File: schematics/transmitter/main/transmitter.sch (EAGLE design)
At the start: 103 parts, among them Q1 16MHz, Q2 P_MOSFET, T1 BC337, T2 BC337, T3 BC337, T4 BC337, U1 EEPROM-I2C, U2 AMS1117_5V, U3 AMS1117_5V, U4 ATMEGA2560AU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

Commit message: Minor improvements (#18)
* Update config.h

* Update eestore.h

* Update eestore.cpp

* Update ui_128x64.cpp

* Add files via upload
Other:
- note added: "NOTES: - MCU pins marked with x have no arduino mapping. They can be used but they have no connector headers on arduino boards, hence have been avoided here. - For two position switches, the UP signal is left unconnected. - The Z1 and Z2 axes as well as X3,Y3,X4,Y4, BTN_A, BTN_B are optional. - Uart0 is used for firmware uploads - Uart1 for interfacing with the secondary mcu (controlling the RF m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"
- note added: "See footnote"
- note added: "The max voltage here should not exceed 4.95V, so the resistors should be sized appropriately. The optocoupler is simply acting as a switch. The usual voltage divider formula still applies. Vsense=Vbat*R2/(R1+R2) E.g. for a 2s Li-ion Vbat max is 8.4V, setting R1 3.3k and R2 4.7k gives good measurement."
- note added: "X1"
- note added: "X2"
- note added: "X3"
- note added: "X4"
- note added: "Y1"
- note added: "Y2"
- note added: "Y3"
- note added: "Y4"
- note removed: "NOTES: - MCU pins marked with x have no arduino mapping. They can be used but they have no connector headers on arduino boards, hence have been avoided here. - For two position switches, the UP signal is left unconnected. - The Z axes are optional. - Uart0 is used for firmware uploads - Uart1 for rf modules - Uart2 for sound modules"
- note removed: "PITCH"
- note removed: "ROLL"
- note removed: "THR"
- note removed: "The max voltage here should not exceed 4.9V, so the resistors in this voltage divider should be sized appropriately"
- note removed: "YAW"
- moved on the sheet: C8, C9, SV18, SV19

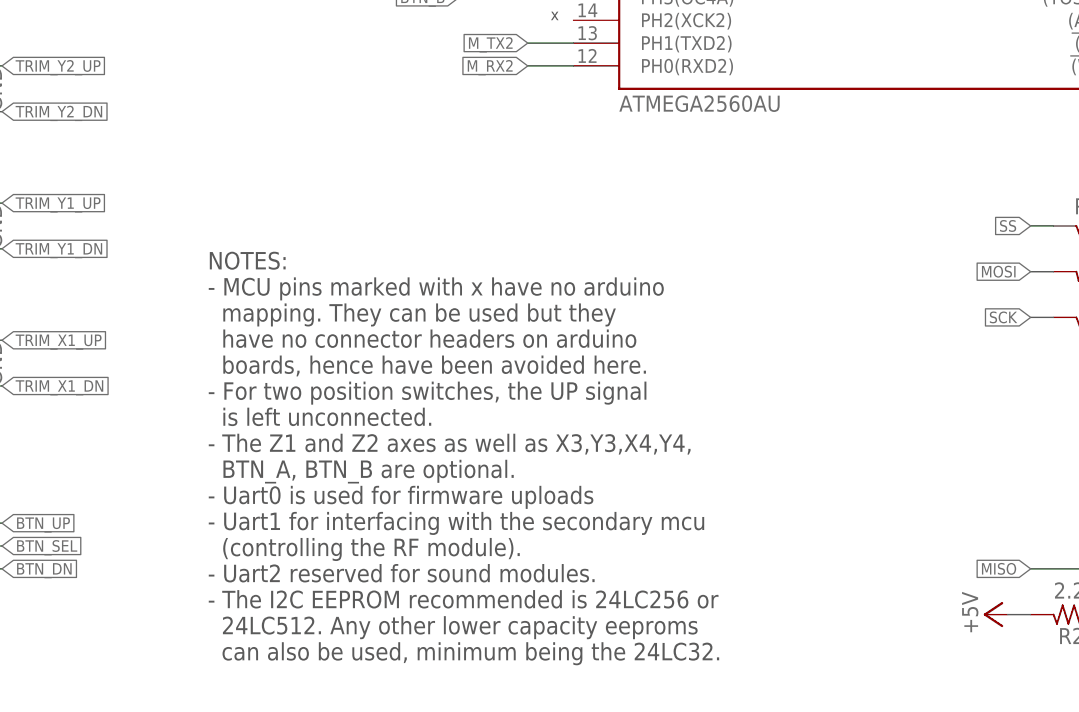
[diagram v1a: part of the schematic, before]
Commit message: Add files via upload
- Update annotations in schematics.
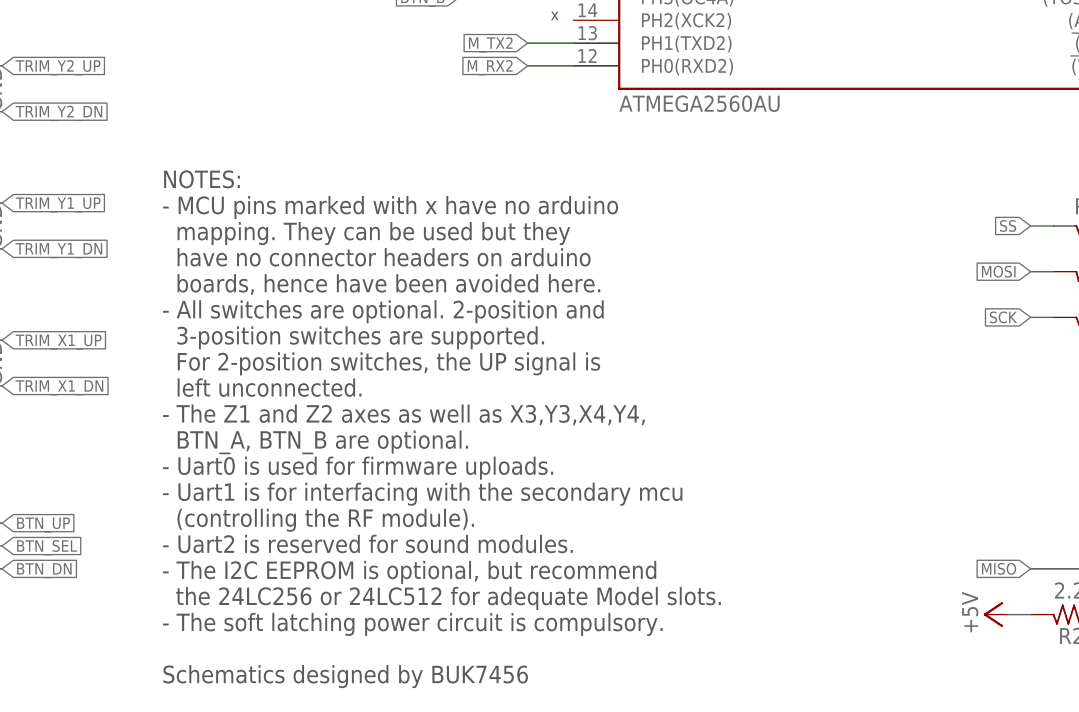
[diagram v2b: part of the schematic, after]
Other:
- note added: "NOTES: - MCU pins marked with x have no arduino mapping. They can be used but they have no connector headers on arduino boards, hence have been avoided here. - All switches are optional. 2-position and 3-position switches are supported. For 2-position switches, the UP signal is left unconnected. - The Z1 and Z2 axes as well as X3,Y3,X4,Y4, BTN_A, BTN_B are optional. - Uart0 is used for firmware u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"
- note removed: "NOTES: - MCU pins marked with x have no arduino mapping. They can be used but they have no connector headers on arduino boards, hence have been avoided here. - For two position switches, the UP signal is left unconnected. - The Z1 and Z2 axes as well as X3,Y3,X4,Y4, BTN_A, BTN_B are optional. - Uart0 is used for firmware uploads - Uart1 for interfacing with the secondary mcu (controlling the RF m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"
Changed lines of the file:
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@@
 <text x="248.92" y="154.94" size="2.54" layer="97">KNOB_B</text>
 <text x="200.66" y="297.18" size="2.54" layer="97">Z2</text>
-<text x="45.72" y="2.54" size="1.9304" layer="97" font="vector">NOTES:
+<text x="40.64" y="0" size="1.9304" layer="97" font="vector">NOTES:
 - MCU pins marked with x have no arduino
   mapping. They can be used but they
   have no connector headers on arduino
   boards, hence have been avoided here.
-- For two position switches, the UP signal
-  is left unconnected.
+- All switches are optional. 2-position and
+  3-position switches are supported.
+  For 2-position switches, the UP signal is
+  left unconnected.
 - The Z1 and Z2 axes as well as X3,Y3,X4,Y4,
   BTN_A, BTN_B are optional.
-- Uart0 is used for firmware uploads
-- Uart1 for interfacing with the secondary mcu
+- Uart0 is used for firmware uploads.
+- Uart1 is for interfacing with the secondary mcu
   (controlling the RF module).
-- Uart2 reserved for sound modules.
-- The I2C EEPROM recommended is 24LC256 or
-  24LC512. Any other lower capacity eeproms
-  can also be used, minimum being the 24LC32.</text>
+- Uart2 is reserved for sound modules.
+- The I2C EEPROM is optional, but recommend
+  the 24LC256 or 24LC512 for adequate Model slots.
+- The soft latching power circuit is compulsory.
+Schematics designed by BUK7456</text>
 <text x="160.02" y="147.32" size="1.27" layer="97">x</text>
 <text x="160.02" y="144.78" size="1.27" layer="97">x</text>
